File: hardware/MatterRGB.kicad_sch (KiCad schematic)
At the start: 51 parts, among them J1 CDM806-04A-MP-F011-67, J2 USB4105, J3 CDM805-08A-FP-F011-67, SW1 NO, SW2 NO, U1 FUSB302B01MPX, U2 ESP32-S3-WROOM-1U-N8R8, U3 DRV8955, U5 LMR51610YFDBVR

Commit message: Finished draft layout of muCM update.
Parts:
- removed C1: 22nF, Capacitor_SMD:C_0805_2012Metric, symbol partywagon112_partdb:KAS21KR71H223KU
- removed C10, C11, C12, C14, C9: 10 nF, Resistor_SMD:R_0603_1608Metric, symbol partywagon112_partdb:GCM188R71H103KA37D
- removed C15, C16: 5.6n, Capacitor_SMD:C_0402_1005Metric, symbol partywagon112_partdb:GCM155R71H562KA55D
- removed C2: 220nF, Capacitor_SMD:C_0603_1608Metric, symbol partywagon112_partdb:GCM188R71H224KA64D
- removed C29: 10uF, Capacitor_SMD:C_0805_2012Metric, symbol partywagon112_fred_partdb:CGA4J1X7S1C106K125AE
- removed C3, C5: 100n, Capacitor_SMD:C_0805_2012Metric, symbol partywagon112_partdb:KAS21KR72A104KU
- removed C31: 220nF, Capacitor_SMD:C_0603_1608Metric, symbol partywagon112_fred_partdb:GCM188R71H224KA64D
- removed D1, D4: RCLAMP0582B.TCT, Package_TO_SOT_SMD:SOT-416, symbol partywagon112_partdb:RCLAMP0582B.TCT
- removed LED2: Red, LED_SMD:LED_0603_1608Metric, symbol partywagon112_fred_partdb:150060SS75020
- removed R2: 2k, Resistor_SMD:R_0402_1005Metric, symbol partywagon112_fred_partdb:CR0402AFX-2001GAS
- removed R7, R8: 10k, Resistor_SMD:R_0402_1005Metric, symbol partywagon112_partdb:CR0402AFX-1002GAS
- removed SW1, SW2: NO, Button_Switch_SMD:SW_Push_1P1T-SH_NO_CK_KMR2xxG, symbol partywagon112_partdb:KMR221G LFS
- removed U2: ESP32-S3-WROOM-1U-N8R8, RF_Module:ESP32-S3-WROOM-1U, symbol partywagon112_partdb:ESP32-S3-WROOM-1U-N8R8
- added C1: 22nF, Capacitor_SMD:C_0603_1608Metric, symbol partywagon112_partdb:CL10B223KC8WPNC
- added C10, C11, C12, C9: 47nF, Capacitor_SMD:C_0603_1608Metric, symbol partywagon112_partdb:CGA3E3X7S2A473K080AE
- added C14: 10nF, Capacitor_SMD:C_0603_1608Metric, symbol partywagon112_partdb:CL10B103KC8WPNC
- added C2: 220nF, Capacitor_SMD:C_0603_1608Metric, symbol partywagon112_partdb:HMK107C7224MAHTE
- added C20: 1u, Capacitor_SMD:C_0603_1608Metric, symbol partywagon112_partdb:GRT188R61H105KE13D
- added C21, C23, C3, C5: 100nF, Capacitor_SMD:C_0603_1608Metric, symbol partywagon112_partdb:GCJ188R72A104KA01D
- added C29: 10 uF, Capacitor_SMD:C_0603_1608Metric, symbol partywagon112_partdb:GRT188R61E106ME13D
- added D1: ESDCAN03, PCM_PartyWagon112_DFN:DFN1006-3, symbol partywagon112_partdb:ESDCAN03-2BM3Y
- added D4: PTVS40VS1UR,115, Diode_SMD:Nexperia_CFP3_SOD-123W, symbol partywagon112_partdb:PTVS40VS1UR,115
- added D5, D6: RCLAMP03391PW.C, Diode_SMD:D_SOD-882, symbol partywagon112_partdb:RCLAMP03391PW.C
- added Q1: 2N7002KL3A-TP, Package_DFN_QFN:Diodes_DFN1006-3, symbol partywagon112_partdb:2N7002KL3A-TP
- added R14, R22, R24: 10k, Resistor_SMD:R_0402_1005Metric, symbol partywagon112_partdb:CR0402AFX-1002GAS
- added R23, R25: 4.75k, Resistor_SMD:R_0402_1005Metric, symbol partywagon112_partdb:CR0402AFX-4751GAS
- added U2: TCAN3413DRBR, Package_SON:VSON-8-1EP_3x3mm_P0.65mm_EP1.6x2.4mm, symbol partywagon112_partdb:TCAN3413DRBR
- added U6: TPS7B4255DBVR, Package_TO_SOT_SMD:SOT-23-5, symbol partywagon112_partdb:TPS7B4255DBVR
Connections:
- net +3V3: now also C13.2, C29.1, R14.1, U2.3 (VCC), U2.5 (VIO); no longer C13.1, C17.1, U1.12 (VCONN), U1.13 (VCONN)
- net CPH: now also C1.1
- net CPL: now also C1.2
- net GND: now also C13.1, C10.2, C11.2, C12.2, C14.2, C20.2, C21.2, C23.2, C29.2, C3.2, C5.2, C9.2, D1.3 (common), D4.2 (A), D5.1 (A1), D6.1 (A1), Q1.2 (S), R23.2, R25.2, U2.2 (GND), U6.2 (GND); no longer C13.2
- net OUT1: now also C10.1
- net OUT2: now also C9.1
- net OUT3: now also C12.1
- net OUT4: now also C11.1
- net USB_D+: now also D6.2 (A2)
- net USB_D-: now also D5.2 (A2)
- net VBUS: now also C3.1
- net VCP: now also C2.1
- net VDC: now also C14.1, C2.2, C21.1, C23.1, D4.1 (K), U6.3 (IN)
- net VDC_F: now also C5.1
- net ~{SLEEP}: now also Q1.3 (D), R14.2, U6.1 (ADJ/EN)
- net CAN+: now reaches J1.3 (Pin_3)
- net CAN+: now also D1.1 (A1), U2.7 (CANH)
- net CAN-: now reaches J1.4 (Pin_4)
- net CAN-: now also D1.2 (A2), U2.6 (CANL)
- net RSVD/EN1 renamed RSVD/EN1
- net TOFF/EN2 renamed TOFF/EN2
- net VBAT_MEAS renamed VMEAS_IN
- net VREF12/EN3: no longer names the net of U3.13 (VREF12/EN3)
- net VREF12/EN3: now also R22.1, R23.1
- net VREF12/EN4: no longer names the net of U3.12 (VREF34/EN4)
- net VREF12/EN4: now also R24.2, R25.1
- new net +3.3VP: C17.1, C20.1, U1.12 (VCONN), U1.13 (VCONN), U6.4 (OUT)
- new net MCU/BOOT/CANTX: U2.1 (TXD)
- new net MCU/CANRX: U2.4 (RXD)
- new net SLEEP: Q1.1 (G), U2.8 (S)
- new net VREF12/EN3: R22.2
- new net VREF12/EN4: R24.1
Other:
- added sheet MCU (mcu.kicad_sch)
- moved on the sheet: C17, C19, C4, C6, C7, R1, R10, R11, R18, R19, R4, R9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

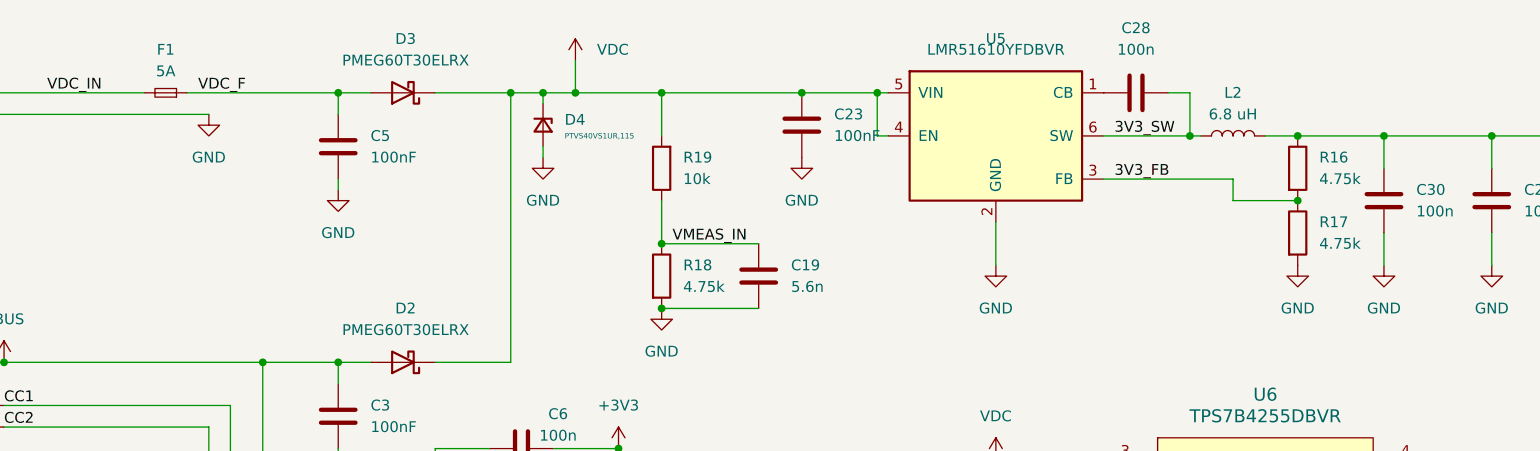
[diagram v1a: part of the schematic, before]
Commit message: removed backups
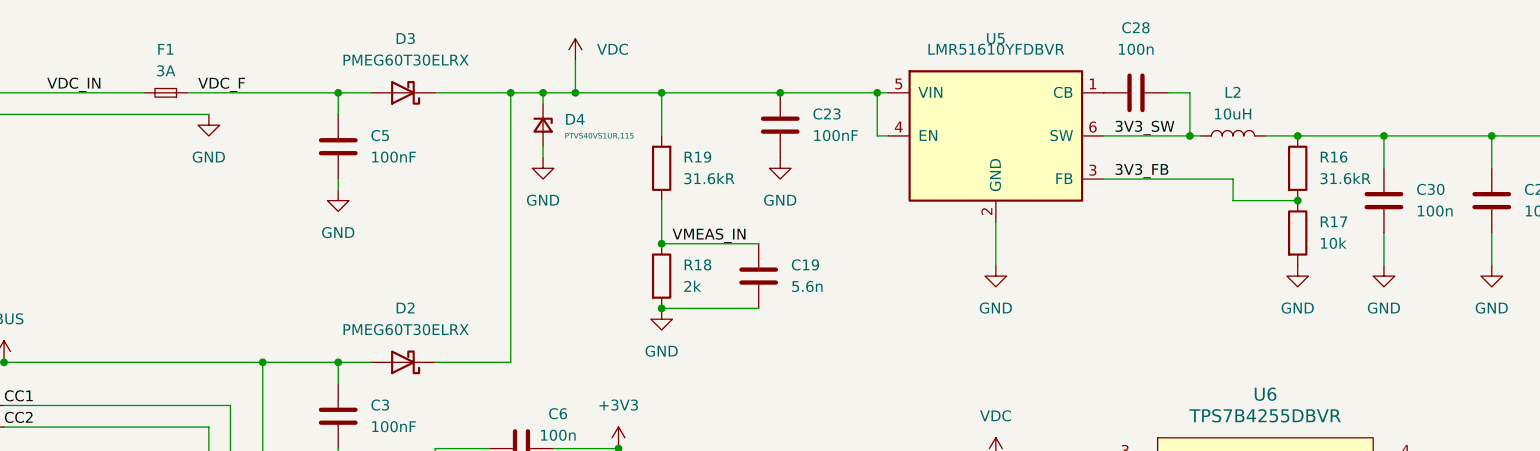
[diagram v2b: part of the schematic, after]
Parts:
- removed F1: 5A, Fuse:Fuse_0805_2012Metric, symbol partywagon112_partdb:MFU0805FF05000P100
- removed L2: 6.8 uH, Inductor_SMD:L_1008_2520Metric, symbol partywagon112_fred_partdb:SRN2510BTA-6R8M
- removed R16, R17, R18: 4.75k, Resistor_SMD:R_0402_1005Metric, symbol partywagon112_partdb:CR0402AFX-4751GAS
- removed R19: 10k, Resistor_SMD:R_0402_1005Metric, symbol partywagon112_partdb:CR0402AFX-1002GAS
- added F1: 3A, Fuse:Fuse_0805_2012Metric, symbol partywagon112_partdb:MFU0805FF03000P100
- added L2: 10uH, Inductor_SMD:L_1008_2520Metric, symbol partywagon112_partdb:SRN2510BTA-100M
- added R16, R19: 31.6kR, Resistor_SMD:R_0402_1005Metric, symbol partywagon112_partdb:CRCW040231K6FKED
- added R17: 10k, Resistor_SMD:R_0402_1005Metric, symbol partywagon112_partdb:CR0402AFX-1002GAS
- added R18: 2k, Resistor_SMD:R_0402_1005Metric, symbol partywagon112_fred_partdb:CR0402AFX-2001GAS
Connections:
- net +3V3: now also L2.2, R16.1
- net 3V3_FB: now also R16.2, R17.1
- net 3V3_SW: now also L2.1
- net GND: now also R17.2, R18.2
- net VDC: now also R19.2
- net VDC_F: now also F1.1
- net VDC_IN: now also F1.2
- net VMEAS_IN: now also R18.1, R19.1
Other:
- moved on the sheet: C23
